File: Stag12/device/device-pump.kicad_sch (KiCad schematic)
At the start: 1 part

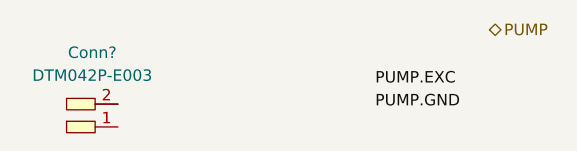
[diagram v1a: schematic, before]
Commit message: Changed EXCs to PWRs
any mention of exc switched to pwr :)
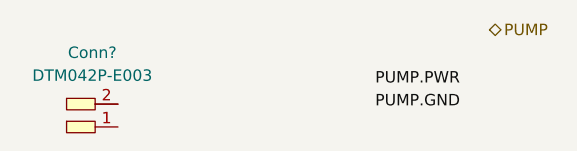
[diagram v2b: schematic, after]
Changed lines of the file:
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@@
 		)
 	)
-	(label "PUMP.EXC"
+	(label "PUMP.PWR"
 		(at 162.56 82.55 0)
 		(effects
